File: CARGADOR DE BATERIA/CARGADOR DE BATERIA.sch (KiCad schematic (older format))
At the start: 11 parts

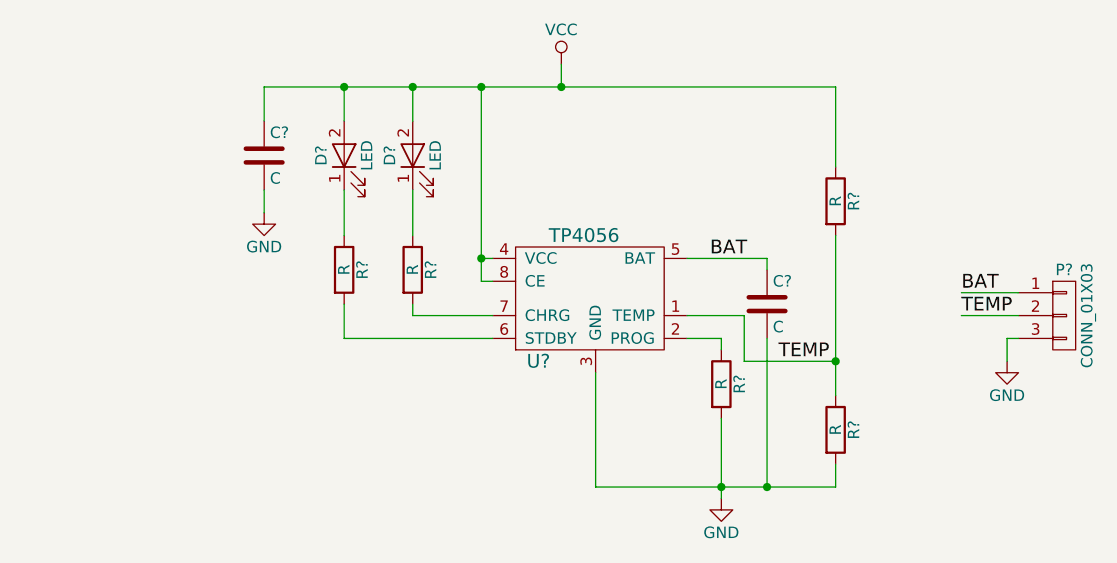
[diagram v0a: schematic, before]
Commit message: agregando el pcb
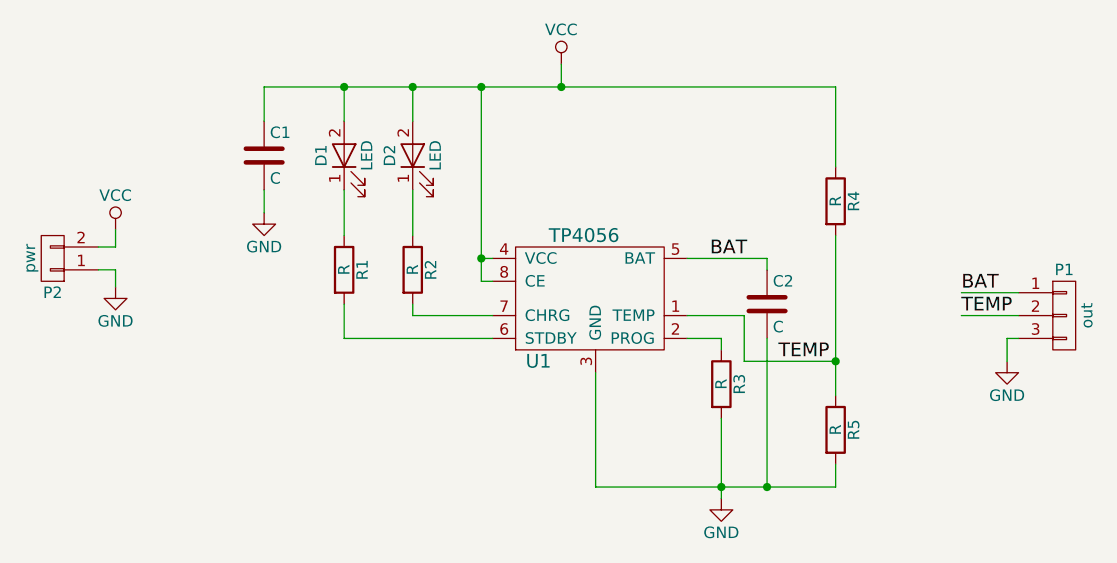
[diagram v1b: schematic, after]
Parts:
- added P2: pwr, Pin_Headers:Pin_Header_Straight_1x02, symbol CONN_01X02
- C1, C2: renamed from C?; footprint (none) -> Capacitors_ThroughHole:C_Disc_D3_P2.5
- D1, D2: renamed from D?; footprint (none) -> LEDs:LED-3MM
- P1: renamed from P?; value CONN_01X03 -> out; footprint (none) -> Pin_Headers:Pin_Header_Straight_1x03
- R1, R2, R3, R4, R5: renamed from R?; footprint (none) -> Resistors_ThroughHole:Resistor_Horizontal_RM7mmJJ
- U1: renamed from U?; footprint (none) -> kicad-libraries:SOP8
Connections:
- net GND: now also P2.1 (P1)
- net VCC: now also P2.2 (P2)
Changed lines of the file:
@@
 LIBS:valves
 LIBS:fuentes
+LIBS:CARGADOR DE BATERIA-cache
 EELAYER 25 0
 EELAYER END
@@
 $EndDescr
 $Comp
-L TP4056 U?
+L TP4056 U1
 U 1 1 595E5DBC
 P 5350 4000
-F 0 "U?" H 5100 3700 60  0000 C CNN
+F 0 "U1" H 5100 3700 60  0000 C CNN
 F 1 "TP4056" H 5300 4250 60  0000 C CNN
-F 2 "" H 4900 3850 60  0001 C CNN
+F 2 "kicad-libraries:SOP8" H 4900 3850 60  0001 C CNN
 F 3 "" H 4900 3850 60  0001 C CNN
 	1    5350 4000
@@
 $EndComp
 $Comp
-L R R?
+L R R2
 U 1 1 595E5E98
 P 4550 3900
-F 0 "R?" V 4630 3900 50  0000 C CNN
+F 0 "R2" V 4630 3900 50  0000 C CNN
 F 1 "R" V 4550 3900 50  0000 C CNN
-F 2 "" V 4480 3900 50  0000 C CNN
+F 2 "Resistors_ThroughHole:Resistor_Horizontal_RM7mmJJ" V 4480 3900 50  0001 C CNN
 F 3 "" H 4550 3900 50  0000 C CNN
 	1    4550 3900
@@
 $EndComp
 $Comp
-L R R?
+L R R1
 U 1 1 595E5EF7
 P 4250 3900
-F 0 "R?" V 4330 3900 50  0000 C CNN
+F 0 "R1" V 4330 3900 50  0000 C CNN
 F 1 "R" V 4250 3900 50  0000 C CNN
-F 2 "" V 4180 3900 50  0000 C CNN
+F 2 "Resistors_ThroughHole:Resistor_Horizontal_RM7mmJJ" V 4180 3900 50  0001 C CNN
 F 3 "" H 4250 3900 50  0000 C CNN
 	1    4250 3900
@@
 	4250 4200 4250 4050
 $Comp
-L LED D?
+L LED D2
 U 1 1 595E5F8C
 P 4550 3400
-F 0 "D?" H 4550 3500 50  0000 C CNN
+F 0 "D2" H 4550 3500 50  0000 C CNN
 F 1 "LED" H 4550 3300 50  0000 C CNN
-F 2 "" H 4550 3400 50  0000 C CNN
+F 2 "LEDs:LED-3MM" H 4550 3400 50  0001 C CNN
 F 3 "" H 4550 3400 50  0000 C CNN
 	1    4550 3400
@@
 $EndComp
 $Comp
-L LED D?
+L LED D1
 U 1 1 595E6009
 P 4250 3400
-F 0 "D?" H 4250 3500 50  0000 C CNN
+F 0 "D1" H 4250 3500 50  0000 C CNN
 F 1 "LED" H 4250 3300 50  0000 C CNN
-F 2 "" H 4250 3400 50  0000 C CNN
+F 2 "LEDs:LED-3MM" H 4250 3400 50  0001 C CNN
 F 3 "" H 4250 3400 50  0000 C CNN
 	1    4250 3400
@@
 Connection ~ 4850 3850
 $Comp
-L C C?
+L C C1
 U 1 1 595E6309
 P 3900 3400
-F 0 "C?" H 3925 3500 50  0000 L CNN
+F 0 "C1" H 3925 3500 50  0000 L CNN
 F 1 "C" H 3925 3300 50  0000 L CNN
-F 2 "" H 3938 3250 50  0000 C CNN
+F 2 "Capacitors_ThroughHole:C_Disc_D3_P2.5" H 3938 3250 50  0001 C CNN
 F 3 "" H 3900 3400 50  0000 C CNN
 	1    3900 3400
@@
 Connection ~ 4250 3100
 $Comp
-L GND #PWR?
+L GND #PWR01
 U 1 1 595E643B
 P 3900 3650
-F 0 "#PWR?" H 3900 3400 50  0001 C CNN
+F 0 "#PWR01" H 3900 3400 50  0001 C CNN
 F 1 "GND" H 3900 3500 50  0000 C CNN
 F 2 "" H 3900 3650 50  0000 C CNN
@@
 	3900 3650 3900 3550
 $Comp
-L C C?
+L C C2
 U 1 1 595E6582
 P 6100 4050
-F 0 "C?" H 6125 4150 50  0000 L CNN
+F 0 "C2" H 6125 4150 50  0000 L CNN
 F 1 "C" H 6125 3950 50  0000 L CNN
-F 2 "" H 6138 3900 50  0000 C CNN
+F 2 "Capacitors_ThroughHole:C_Disc_D3_P2.5" H 6138 3900 50  0001 C CNN
 F 3 "" H 6100 4050 50  0000 C CNN
 	1    6100 4050
@@
 	6100 3850 5750 3850
 $Comp
-L R R?
+L R R3
 U 1 1 595E661C
 P 5900 4400
-F 0 "R?" V 5980 4400 50  0000 C CNN
+F 0 "R3" V 5980 4400 50  0000 C CNN
 F 1 "R" V 5900 4400 50  0000 C CNN
-F 2 "" V 5830 4400 50  0000 C CNN
+F 2 "Resistors_ThroughHole:Resistor_Horizontal_RM7mmJJ" V 5830 4400 50  0001 C CNN
 F 3 "" H 5900 4400 50  0000 C CNN
 	1    5900 4400
@@
 	5900 4550 5900 4900
 $Comp
-L GND #PWR?
+L GND #PWR02
 U 1 1 595E676C
 P 5900 4900
-F 0 "#PWR?" H 5900 4650 50  0001 C CNN
+F 0 "#PWR02" H 5900 4650 50  0001 C CNN
 F 1 "GND" H 5900 4750 50  0000 C CNN
 F 2 "" H 5900 4900 50  0000 C CNN
@@
 	5350 4850 5350 4350
 $Comp
-L R R?
+L R R4
 U 1 1 595E6996
 P 6400 3600
-F 0 "R?" V 6480 3600 50  0000 C CNN
+F 0 "R4" V 6480 3600 50  0000 C CNN
 F 1 "R" V 6400 3600 50  0000 C CNN
-F 2 "" V 6330 3600 50  0000 C CNN
+F 2 "Resistors_ThroughHole:Resistor_Horizontal_RM7mmJJ" V 6330 3600 50  0001 C CNN
 F 3 "" H 6400 3600 50  0000 C CNN
 	1    6400 3600
@@
 $EndComp
 $Comp
-L R R?
+L R R5
 U 1 1 595E69E3
 P 6400 4600
-F 0 "R?" V 6480 4600 50  0000 C CNN
+F 0 "R5" V 6480 4600 50  0000 C CNN
 F 1 "R" V 6400 4600 50  0000 C CNN
-F 2 "" V 6330 4600 50  0000 C CNN
+F 2 "Resistors_ThroughHole:Resistor_Horizontal_RM7mmJJ" V 6330 4600 50  0001 C CNN
 F 3 "" H 6400 4600 50  0000 C CNN
 	1    6400 4600
@@
 TEMP
 $Comp
-L CONN_01X03 P?
+L CONN_01X03 P1
 U 1 1 595E827A
 P 7400 4100
-F 0 "P?" H 7400 4300 50  0000 C CNN
-F 1 "CONN_01X03" V 7500 4100 50  0000 C CNN
-F 2 "" H 7400 4100 50  0000 C CNN
+F 0 "P1" H 7400 4300 50  0000 C CNN
+F 1 "out" V 7500 4100 50  0000 C CNN
+F 2 "Pin_Headers:Pin_Header_Straight_1x03" H 7400 4100 50  0001 C CNN
 F 3 "" H 7400 4100 50  0000 C CNN
 	1    7400 4100
@@
 TEMP
 $Comp
-L GND #PWR?
+L GND #PWR03
 U 1 1 595E8819
 P 7150 4300
-F 0 "#PWR?" H 7150 4050 50  0001 C CNN
+F 0 "#PWR03" H 7150 4050 50  0001 C CNN
 F 1 "GND" H 7150 4150 50  0000 C CNN
 F 2 "" H 7150 4300 50  0000 C CNN
@@
 	7150 4200 7150 4300
 $Comp
-L VCC #PWR?
+L VCC #PWR04
 U 1 1 595E8F68
 P 5200 3000
-F 0 "#PWR?" H 5200 2850 50  0001 C CNN
+F 0 "#PWR04" H 5200 2850 50  0001 C CNN
 F 1 "VCC" H 5200 3150 50  0000 C CNN
 F 2 "" H 5200 3000 50  0000 C CNN
@@
 	5200 3000 5200 3100
 Connection ~ 5200 3100
+$Comp
+L CONN_01X02 P2
+U 1 1 595E7ECD
+P 2975 3850
+F 0 "P2" H 2975 4000 50  0000 C CNN
+F 1 "pwr" V 3075 3850 50  0000 C CNN
+F 2 "Pin_Headers:Pin_Header_Straight_1x02" H 2975 3850 50  0001 C CNN
+F 3 "" H 2975 3850 50  0000 C CNN
+	1    2975 3850
+	-1   0    0    1
+$EndComp
+$Comp
+L VCC #PWR05
+U 1 1 595E7F8E
+P 3250 3725
+F 0 "#PWR05" H 3250 3575 50  0001 C CNN
+F 1 "VCC" H 3250 3875 50  0000 C CNN
+F 2 "" H 3250 3725 50  0000 C CNN
+F 3 "" H 3250 3725 50  0000 C CNN
+	1    3250 3725
+	1    0    0    -1
+$EndComp
+$Comp
+L GND #PWR06
+U 1 1 595E801A
+P 3250 3975
+F 0 "#PWR06" H 3250 3725 50  0001 C CNN
+F 1 "GND" H 3250 3825 50  0000 C CNN
+F 2 "" H 3250 3975 50  0000 C CNN
+F 3 "" H 3250 3975 50  0000 C CNN
+	1    3250 3975
+	1    0    0    -1
+$EndComp
+Wire Wire Line
+	3250 3975 3250 3900
+Wire Wire Line
+	3250 3900 3175 3900
+Wire Wire Line
+	3250 3725 3250 3800
+Wire Wire Line
+	3250 3800 3175 3800
 $EndSCHEMATC
